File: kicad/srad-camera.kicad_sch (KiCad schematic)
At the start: 15 parts, among them J1 SWD

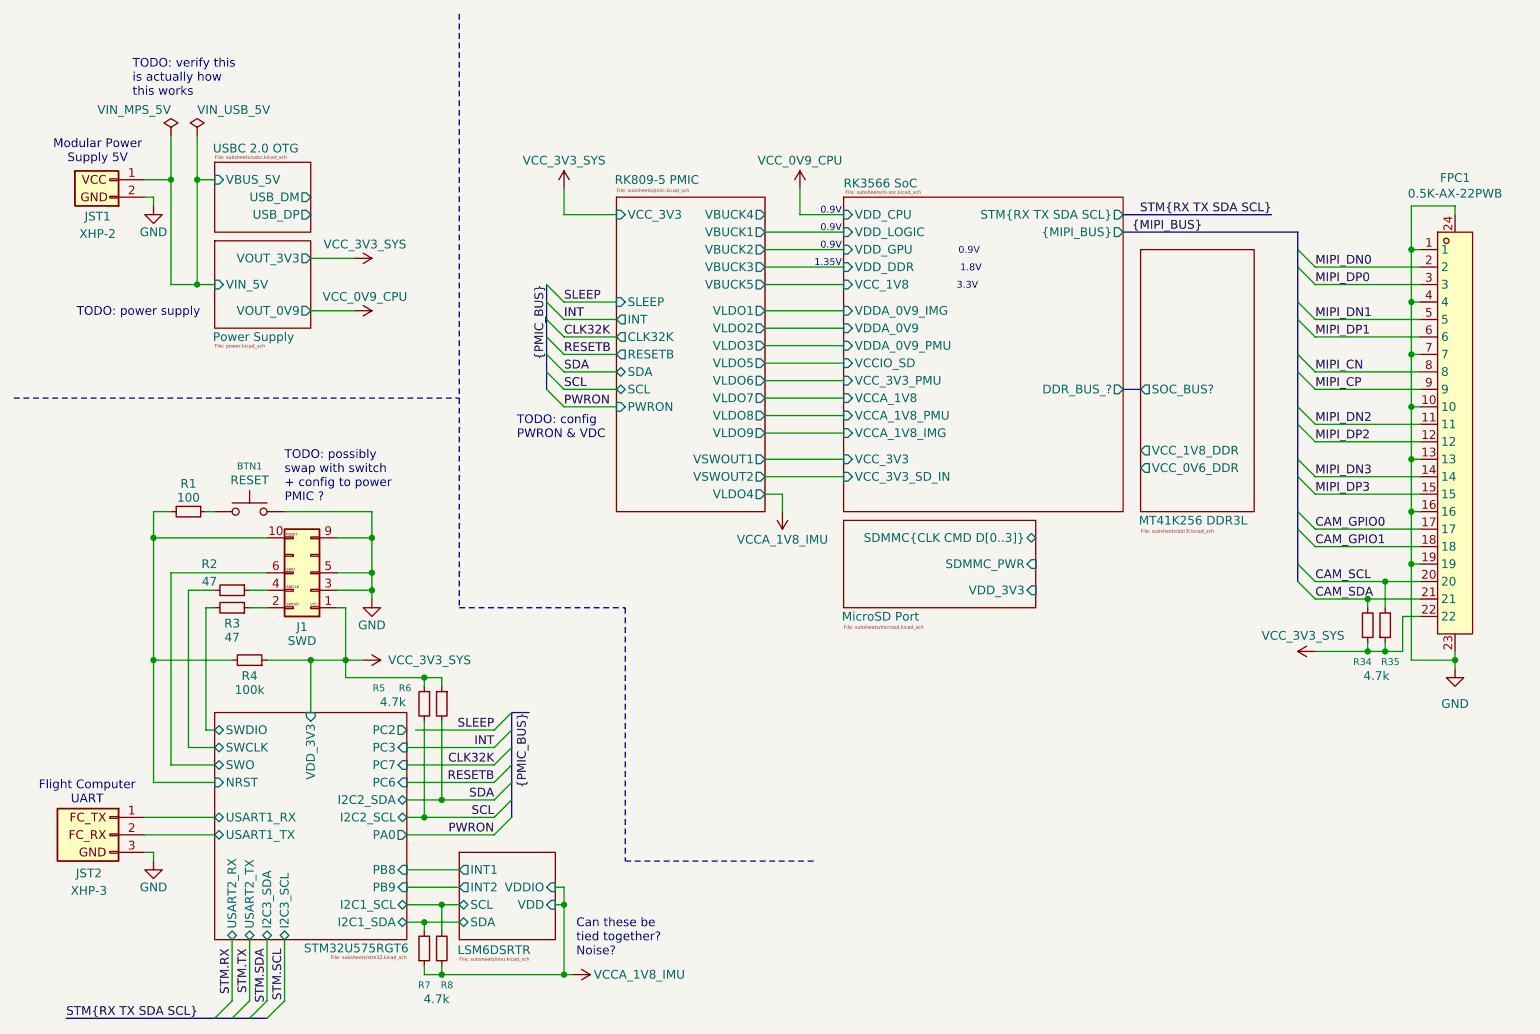
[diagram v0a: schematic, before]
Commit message: Adjust root sheet
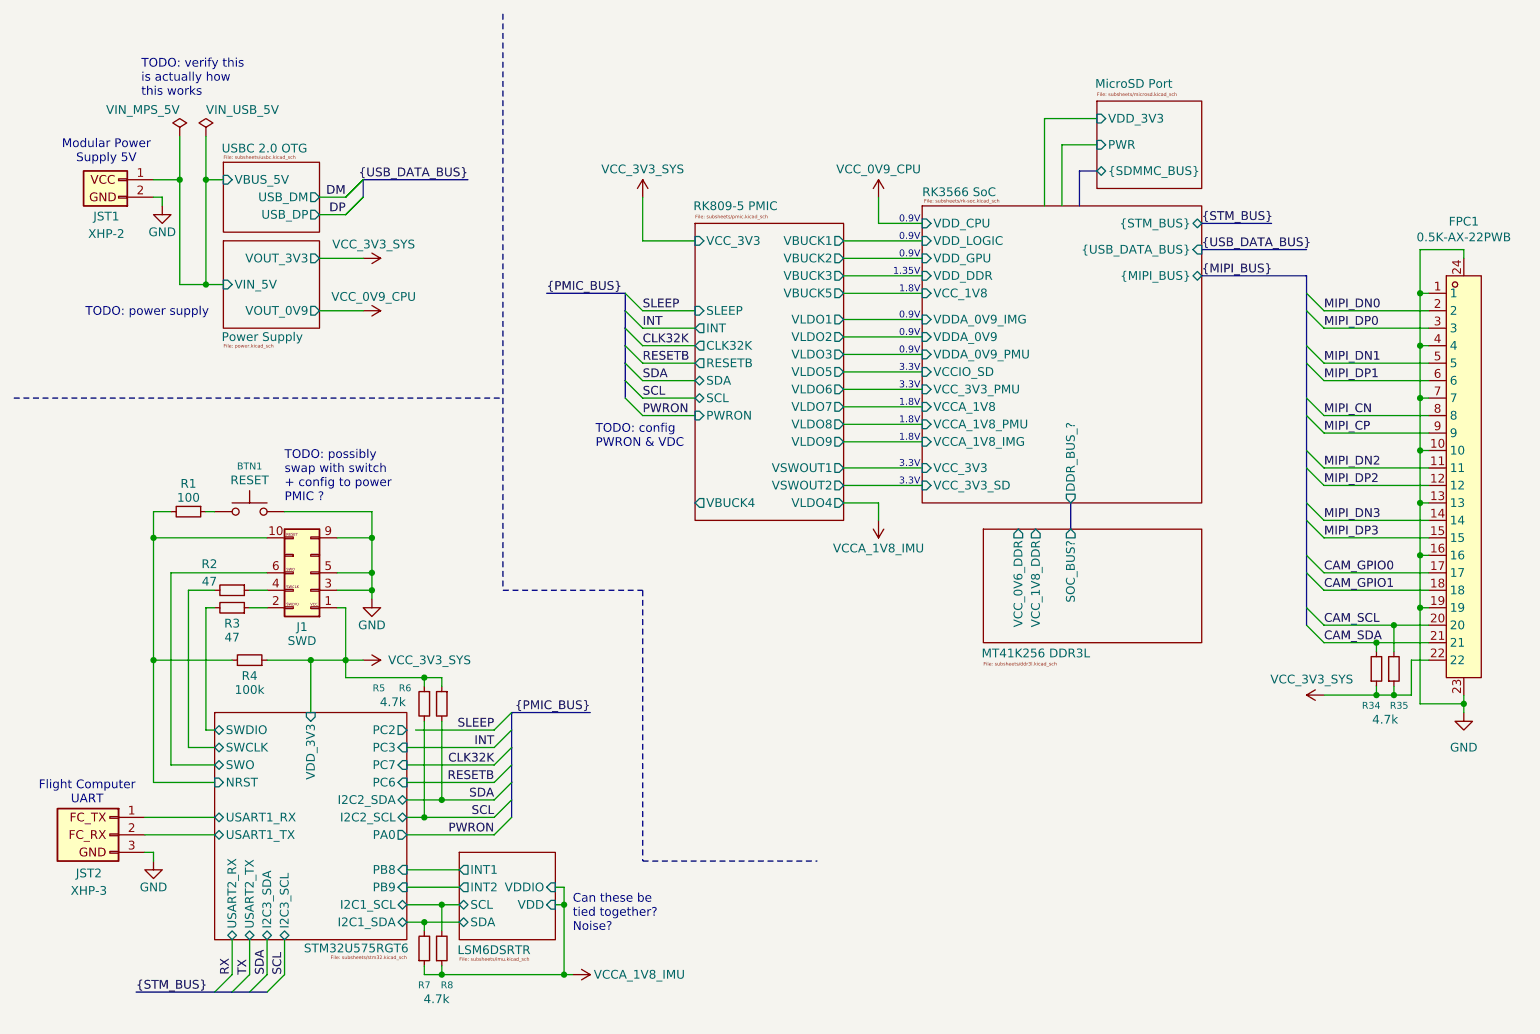
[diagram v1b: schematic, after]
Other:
- sheet MicroSD Port ports: added PWR, {SDMMC_BUS}; removed SDMMC_PWR, SDMMC{CLK CMD D[0..3]}
- sheet RK3566 SoC ports: added VCC_3V3_SD, {STM_BUS}, {USB_DATA_BUS}; removed STM{RX TX SDA SCL}, VCC_3V3_SD_IN
- moved on the sheet: FPC1, JST1, R34, R35

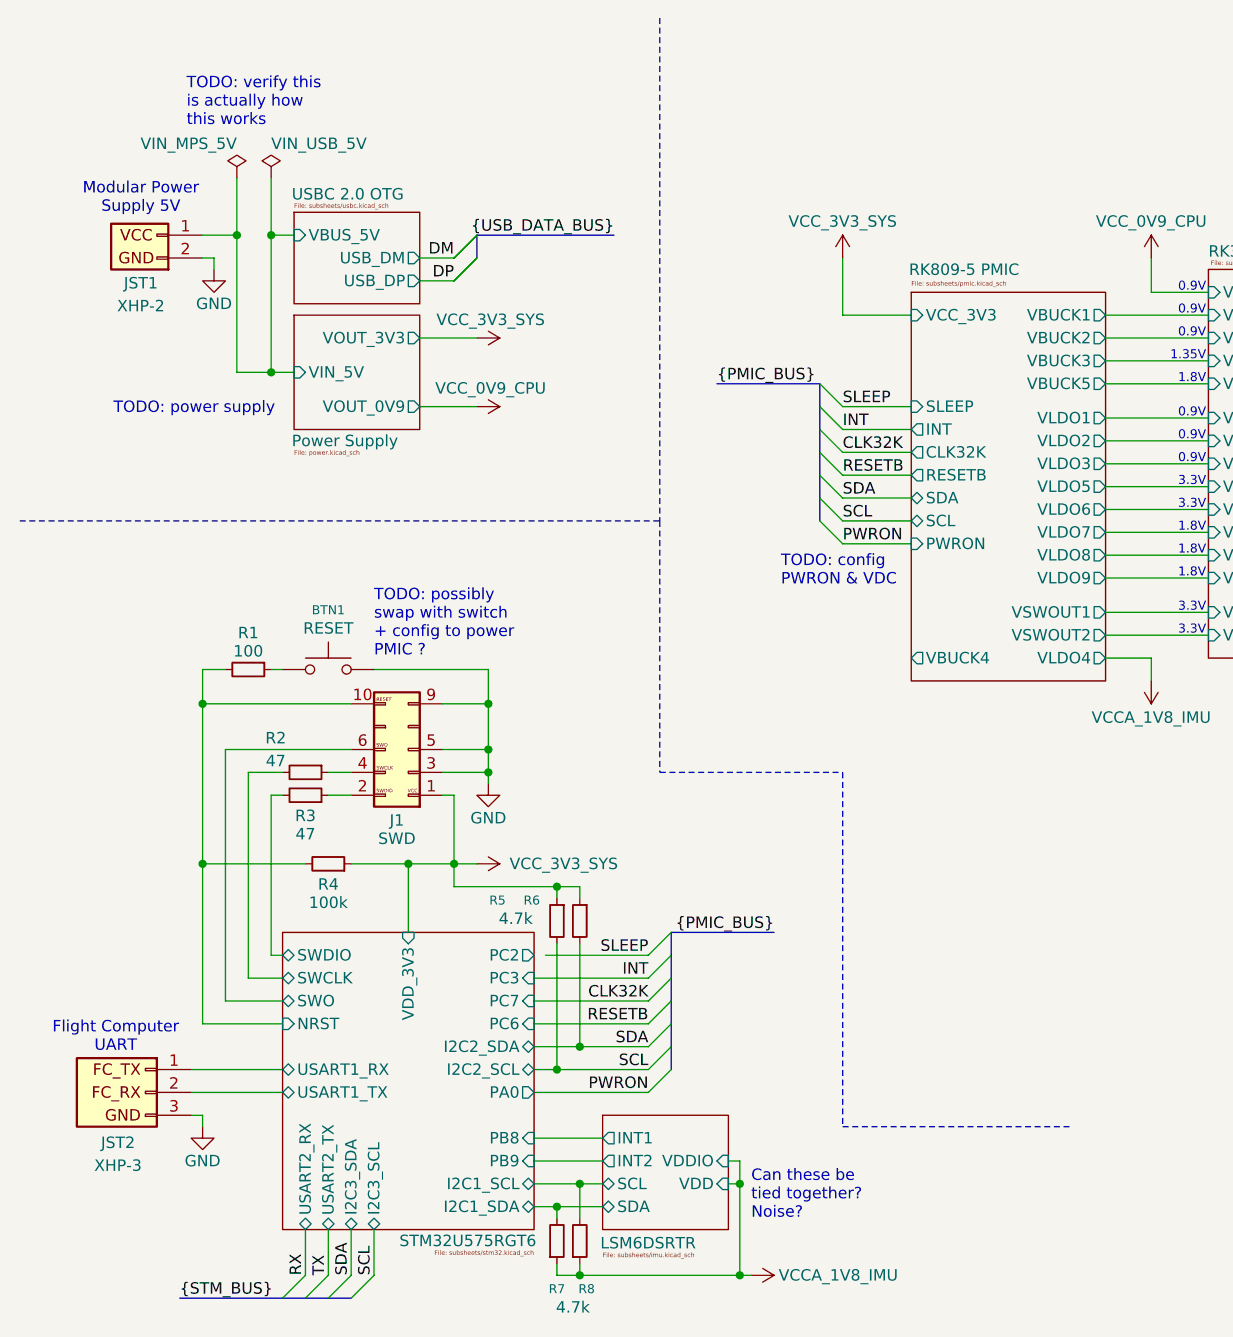
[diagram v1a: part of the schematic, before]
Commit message: Update buck converters
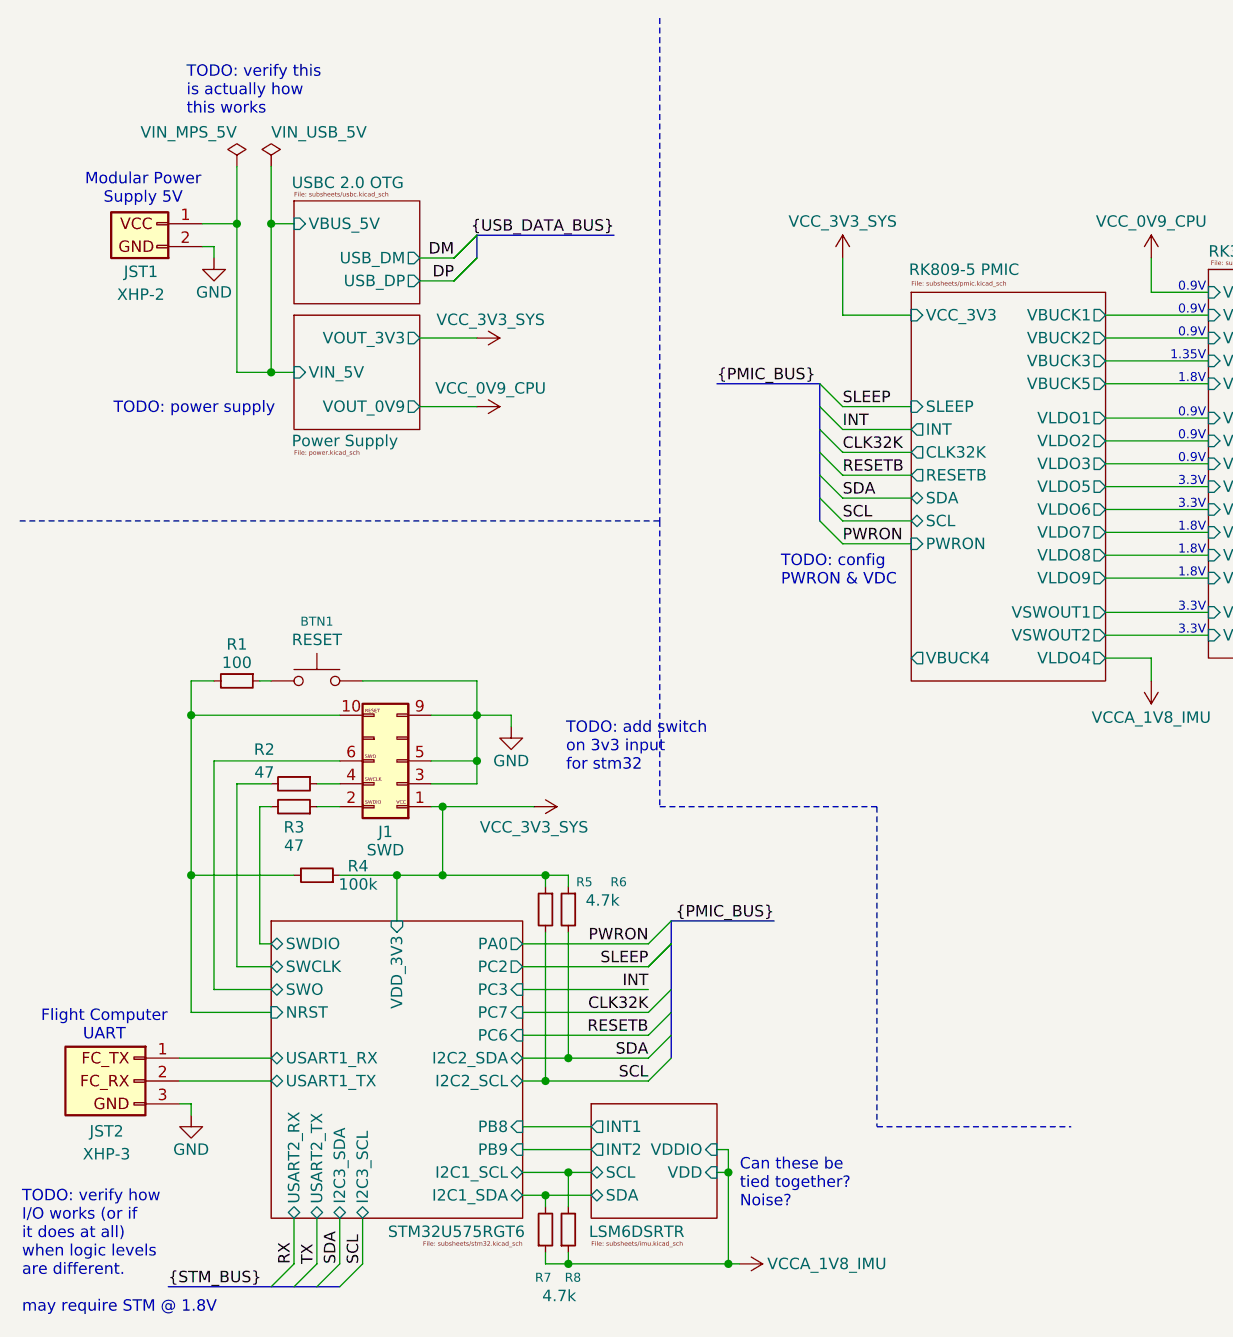
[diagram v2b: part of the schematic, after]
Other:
- note added: "TODO: add switch on 3v3 input for stm32"
- note added: "TODO: verify how I/O works (or if it does at all) when logic levels are different. may require STM @ 1.8V"
- note removed: "TODO: possibly swap with switch + config to power PMIC ?"
- moved on the sheet: BTN1, J1, JST1, JST2, R1, R2, R3, R4, R5, R6, R7, R8

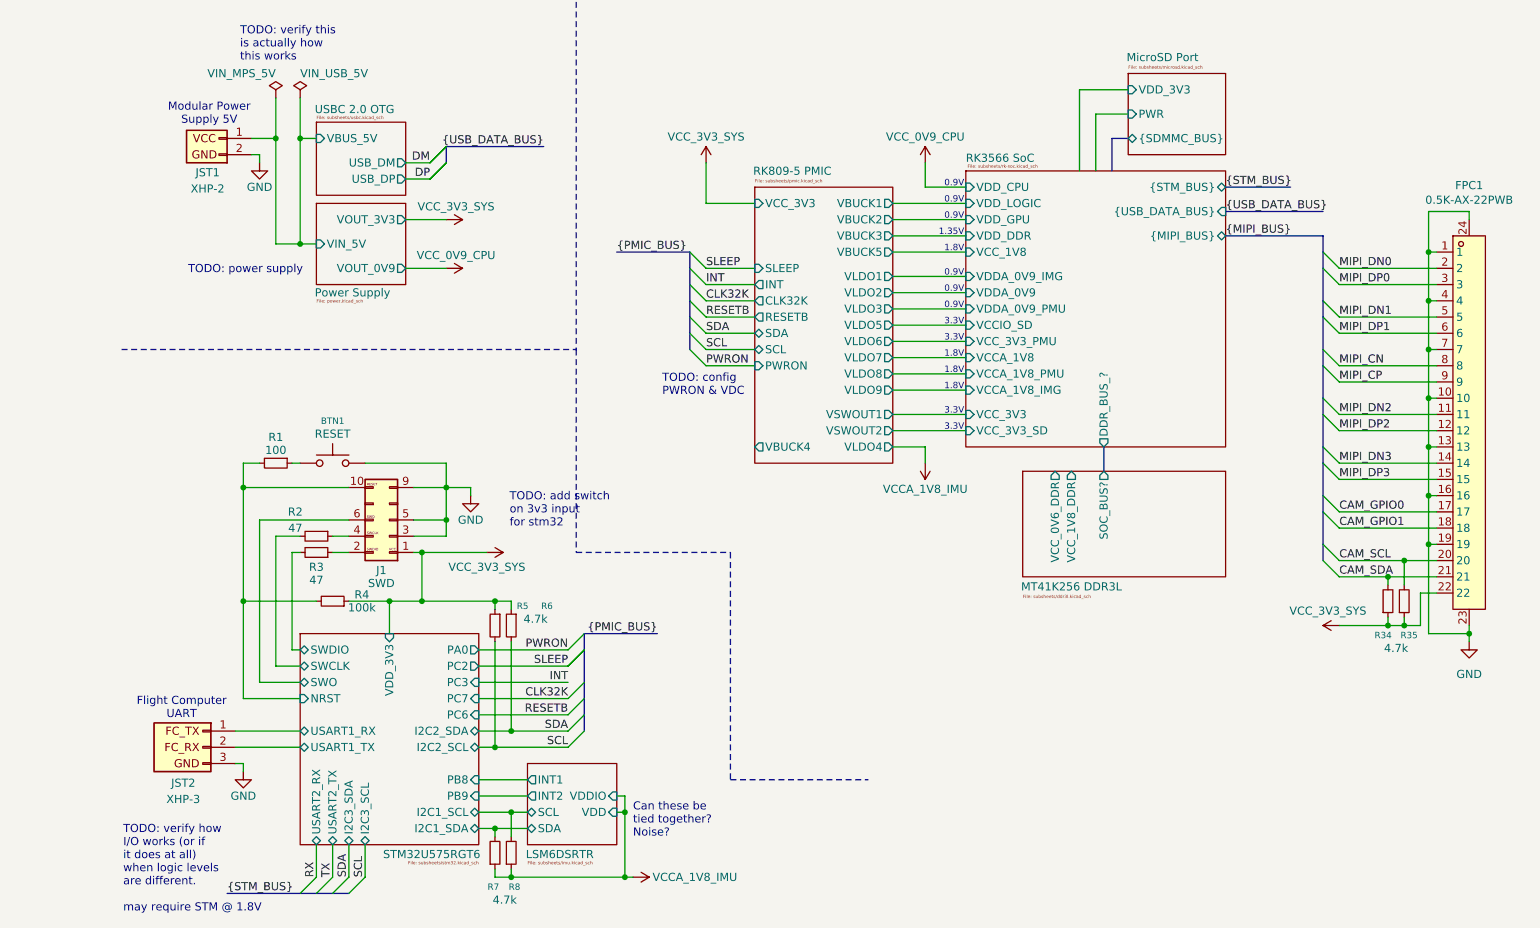
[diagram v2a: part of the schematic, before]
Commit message: Add power supply and ll shifter
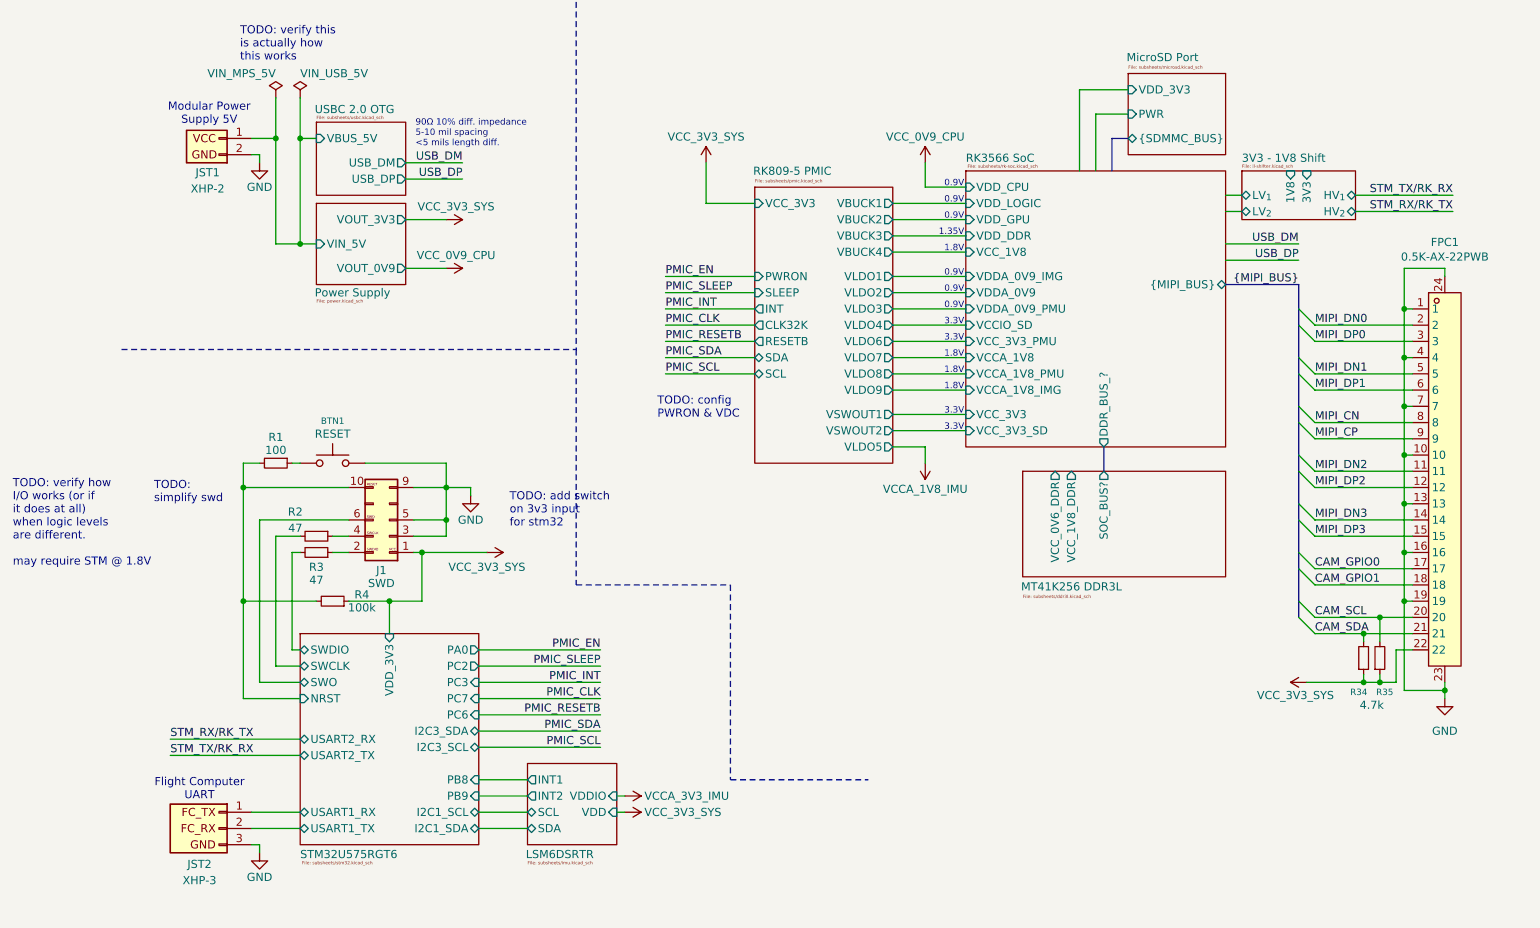
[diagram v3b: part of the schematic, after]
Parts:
- removed R5, R6, R7, R8: 4.7k, symbol Device:R_Small
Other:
- added sheet 3V3 - 1V8 Shift (ll-shifter.kicad_sch)
- sheet RK3566 SoC ports: added none; removed {STM_BUS}, {USB_DATA_BUS}
- sheet RK809-5 PMIC ports: added none; removed VBUCK5
- sheet STM32U575RGT6 ports: added none; removed I2C2_SCL, I2C2_SDA
- note added: "90Ω 10% diff. impedance 5-10 mil spacing <5 mils length diff."
- note added: "TODO: simplify swd"
- note removed: "Can these be tied together? Noise?"
- note removed: "TODO: power supply"
- moved on the sheet: FPC1, JST2, R34, R35
